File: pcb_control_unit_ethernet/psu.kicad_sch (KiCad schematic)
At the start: 21 parts, among them J4 DC IN, J5 USB STM32, U3 DCDC_MP2315, U4 TPS54202DDC, U5 AMS1117-3.3, U6 INA226, X1 MT3608

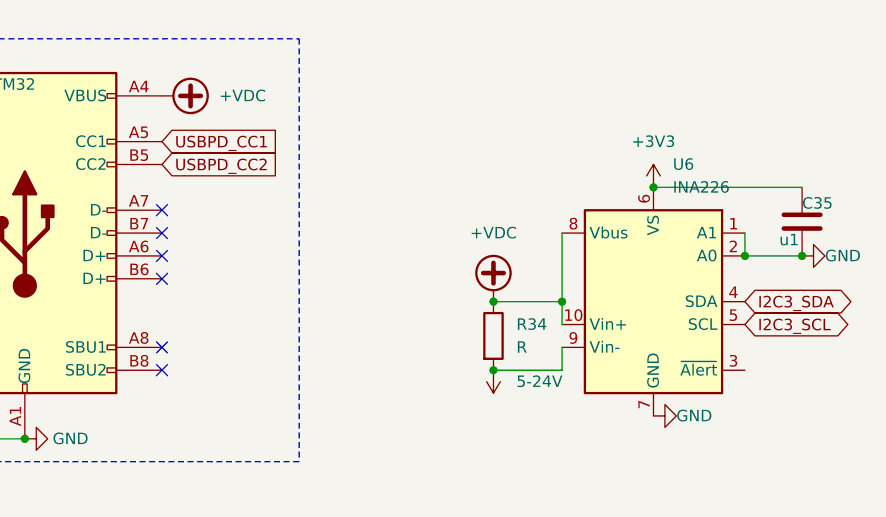
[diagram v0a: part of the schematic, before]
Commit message: First time zero errors, but bad layout
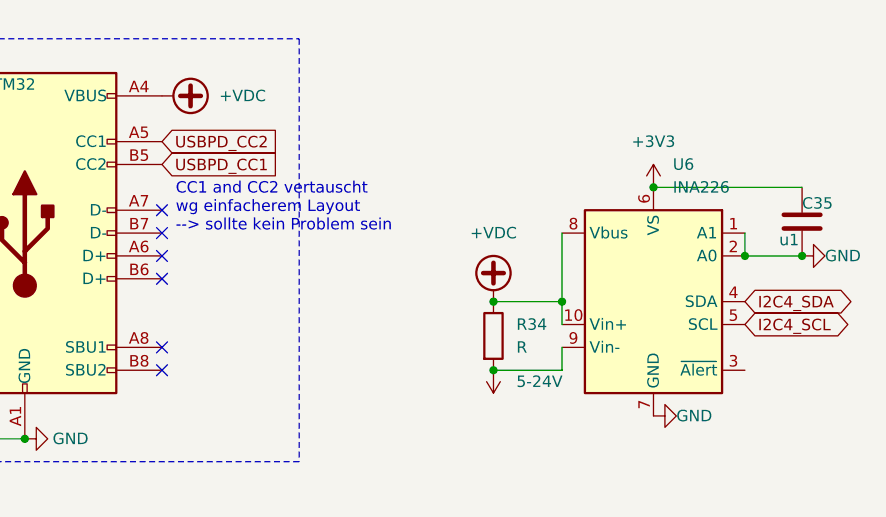
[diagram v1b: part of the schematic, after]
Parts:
- C35: footprint Capacitor_SMD:C_0402_1005Metric -> Capacitor_SMD:C_0201_0603Metric
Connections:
- net USBPD_CC1: now also J5.B5 (CC2); no longer J5.A5 (CC1)
- net USBPD_CC2: now also J5.A5 (CC1); no longer J5.B5 (CC2)
- net I2C3_SCL renamed I2C4_SCL
- net I2C3_SDA renamed I2C4_SDA
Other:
- note added: "CC1 and CC2 vertauscht wg einfacherem Layout --> sollte kein Problem sein"
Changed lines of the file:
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@@
+		)
+	)
+	(text "CC1 and CC2 vertauscht \nwg einfacherem Layout\n--> sollte kein Problem sein"
+		(exclude_from_sim no)
+		(at 141.224 35.306 0)
+		(effects
+			(font
+				(size 1.27 1.27)
+				(color 255 50 76 1)
+			)
+			(justify left)
 		)
 	)
@@
 		)
 	)
-	(global_label "I2C3_SDA"
+	(global_label "I2C4_SDA"
 		(shape bidirectional)
 		(at 204.47 45.72 0)
@@
 	(global_label "USBPD_CC1"
 		(shape input)
+		(at 139.7 30.48 0)
+		(fields_autoplaced yes)
+		(effects
+			(font
+				(size 1.27 1.27)
+			)
+			(justify left)
+		)
+		(property "Intersheetrefs" "${INTERSHEET_REFS}"
+			(at 153.7523 30.48 0)
+			(effects
+				(font
+					(size 1.27 1.27)
+				)
+				(justify left)
+				(hide yes)
+			)
+		)
+	)
+	(global_label "USBPD_CC2"
+		(shape input)
 		(at 139.7 27.94 0)
 		(fields_autoplaced yes)
@@
 		)
 	)
-	(global_label "USBPD_CC2"
-		(shape input)
-		(at 139.7 30.48 0)
-		(fields_autoplaced yes)
-		(effects
-			(font
-				(size 1.27 1.27)
-			)
-			(justify left)
-		)
-		(property "Intersheetrefs" "${INTERSHEET_REFS}"
-			(at 153.7523 30.48 0)
-			(effects
-				(font
-					(size 1.27 1.27)
-				)
-				(justify left)
-				(hide yes)
-			)
-		)
-	)
-	(global_label "I2C3_SCL"
+	(global_label "I2C4_SCL"
 		(shape bidirectional)
 		(at 204.47 48.26 0)
@@
 			)
 		)
-		(property "Footprint" "Capacitor_SMD:C_0402_1005Metric"
+		(property "Footprint" "Capacitor_SMD:C_0201_0603Metric"
 			(at 211.7852 40.64 0)
 			(effects
